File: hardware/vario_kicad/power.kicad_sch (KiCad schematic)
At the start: 28 parts, among them Q1 NMOS, Q2 PMOS, U4 USB C connector

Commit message: add missing footprints
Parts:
- R31, R32: footprint (none) -> Resistor_SMD:R_0402_1005Metric
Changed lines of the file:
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@@
 			)
 		)
-		(property "Footprint" ""
+		(property "Footprint" "Resistor_SMD:R_0402_1005Metric"
 			(at 148.082 72.39 90)
 			(effects
@@
 			)
 		)
-		(property "Footprint" ""
+		(property "Footprint" "Resistor_SMD:R_0402_1005Metric"
 			(at 132.08 38.608 90)
 			(effects

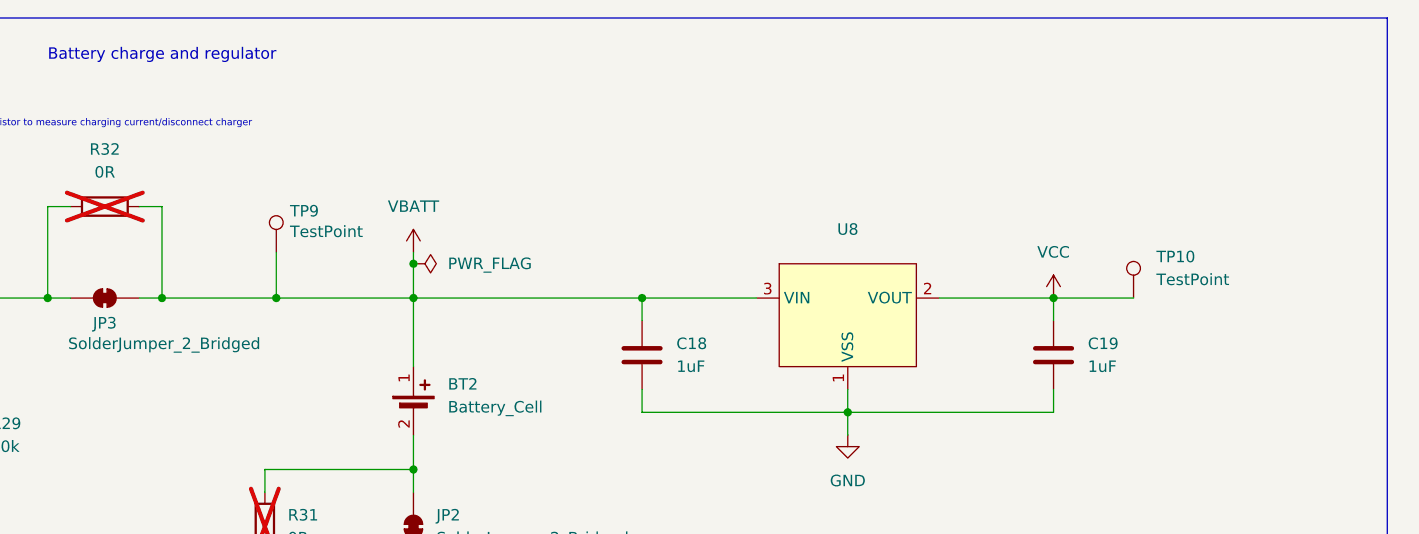
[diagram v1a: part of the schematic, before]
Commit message: remove more testpoints
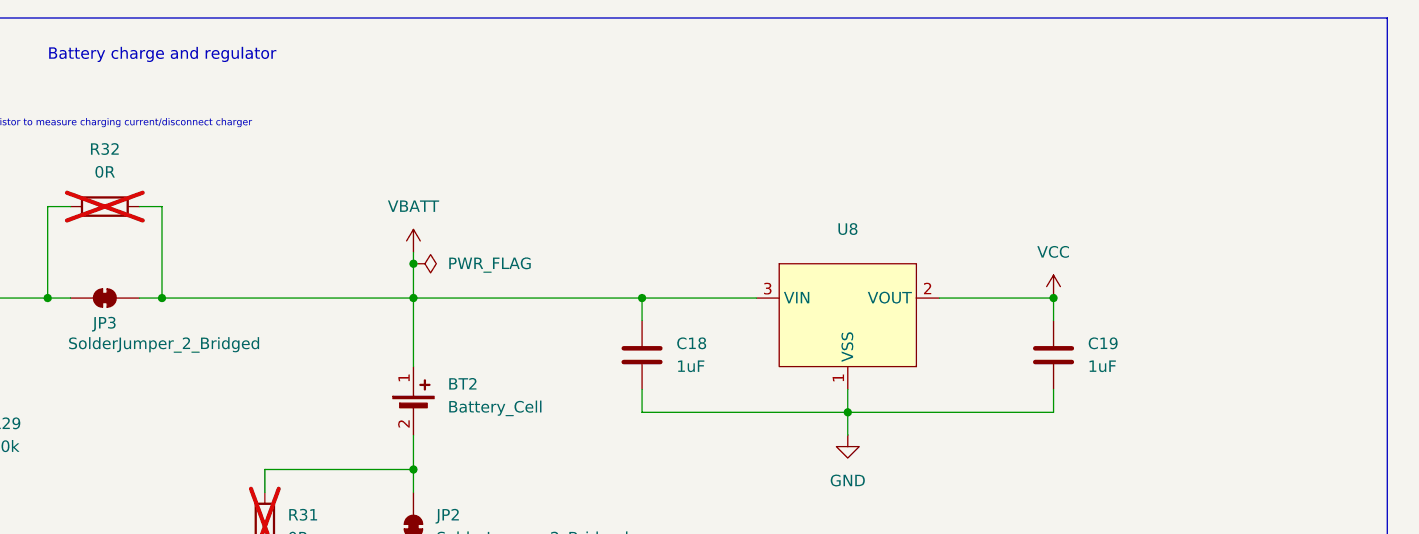
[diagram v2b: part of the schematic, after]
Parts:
- removed TP10, TP9: TestPoint, TestPoint:TestPoint_Pad_D1.0mm, symbol Connector:TestPoint
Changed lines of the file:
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@@
 	)
 	(junction
-		(at 151.13 46.99)
-		(diameter 0)
-		(color 0 0 0 0)
-	)
-	(junction
 		(at 76.2 29.21)
 		(diameter 0)
@@
 	(wire
 		(pts
-			(xy 151.13 41.91) (xy 151.13 46.99)
-		)
-		(stroke
-			(width 0)
-			(type default)
-		)
-	)
-	(wire
-		(pts
 			(xy 237.49 57.15) (xy 237.49 59.69)
 		)
@@
 	(wire
 		(pts
-			(xy 151.13 46.99) (xy 166.37 46.99)
-		)
-		(stroke
-			(width 0)
-			(type default)
-		)
-	)
-	(wire
-		(pts
 			(xy 68.58 137.16) (xy 68.58 140.97)
 		)
@@
 	(wire
 		(pts
-			(xy 237.49 46.99) (xy 246.38 46.99)
-		)
-		(stroke
-			(width 0)
-			(type default)
-		)
-	)
-	(wire
-		(pts
 			(xy 68.58 148.59) (xy 68.58 149.86)
 		)
@@
 	(wire
 		(pts
-			(xy 138.43 46.99) (xy 151.13 46.99)
+			(xy 138.43 46.99) (xy 166.37 46.99)
 		)
 		(stroke
@@
 	)
 	(symbol
-		(lib_id "Connector:TestPoint")
-		(at 246.38 46.99 0)
-		(unit 1)
-		(exclude_from_sim no)
-		(in_bom yes)
-		(on_board yes)
-		(dnp no)
-		(fields_autoplaced yes)
-		(property "Reference" "TP10"
-			(at 248.92 42.4179 0)
-			(effects
-				(font
-					(size 1.27 1.27)
-				)
-				(justify left)
-			)
-		)
-		(property "Value" "TestPoint"
-			(at 248.92 44.9579 0)
-			(effects
-				(font
-					(size 1.27 1.27)
-				)
-				(justify left)
-			)
-		)
-		(property "Footprint" "TestPoint:TestPoint_Pad_D1.0mm"
-			(at 251.46 46.99 0)
-			(effects
-				(font
-					(size 1.27 1.27)
-				)
-				(hide yes)
-			)
-		)
-		(property "Datasheet" "~"
-			(at 251.46 46.99 0)
-			(effects
-				(font
-					(size 1.27 1.27)
-				)
-				(hide yes)
-			)
-		)
-		(property "Description" "test point"
-			(at 246.38 46.99 0)
-			(effects
-				(font
-					(size 1.27 1.27)
-				)
-				(hide yes)
-			)
-		)
-		(property "Sim.Pins" ""
-			(at 246.38 46.99 0)
-			(effects
-				(font
-					(size 1.27 1.27)
-				)
-				(hide yes)
-			)
-		)
-		(pin "1"
-		)
-		(instances
-			(project "vario_kicad"
-				(path "/50389aff-b244-451e-8e3a-c5addd2215e1/9ff7b2dd-70fe-4259-884c-1f1f10c7ad3d"
-					(reference "TP10")
-					(unit 1)
-				)
-			)
-		)
-	)
-	(symbol
 		(lib_id "Device:R")
 		(at 132.08 36.83 90)
@@
 					(unit 1)
 				)
-			)
-		)
-	)
-	(symbol
-		(lib_id "Connector:TestPoint")
-		(at 151.13 41.91 0)
-		(unit 1)
-		(exclude_from_sim no)
-		(in_bom yes)
-		(on_board yes)
-		(dnp no)
-		(property "Reference" "TP9"
-			(at 152.654 37.338 0)
-			(effects
-				(font
-					(size 1.27 1.27)
-				)
-				(justify left)
-			)
-		)
-		(property "Value" "TestPoint"
-			(at 152.654 39.624 0)
-			(effects
-				(font
-					(size 1.27 1.27)
-				)
-				(justify left)
-			)
-		)
-		(property "Footprint" "TestPoint:TestPoint_Pad_D1.0mm"
-			(at 156.21 41.91 0)
-			(effects
-				(font
-					(size 1.27 1.27)
-				)
-				(hide yes)
-			)
-		)
-		(property "Datasheet" "~"
-			(at 156.21 41.91 0)
-			(effects
-				(font
-					(size 1.27 1.27)
-				)
-				(hide yes)
-			)
-		)
-		(property "Description" "test point"
-			(at 151.13 41.91 0)
-			(effects
-				(font
-					(size 1.27 1.27)
-				)
-				(hide yes)
-			)
-		)
-		(property "Sim.Pins" ""
-			(at 151.13 41.91 0)
-			(effects
-				(font
-					(size 1.27 1.27)
-				)
-				(hide yes)
-			)
-		)
-		(pin "1"
-		)
-		(instances
-			(project "vario_kicad"
-				(path "/50389aff-b244-451e-8e3a-c5addd2215e1/9ff7b2dd-70fe-4259-884c-1f1f10c7ad3d"
-					(reference "TP9")
-					(unit 1)
-				)

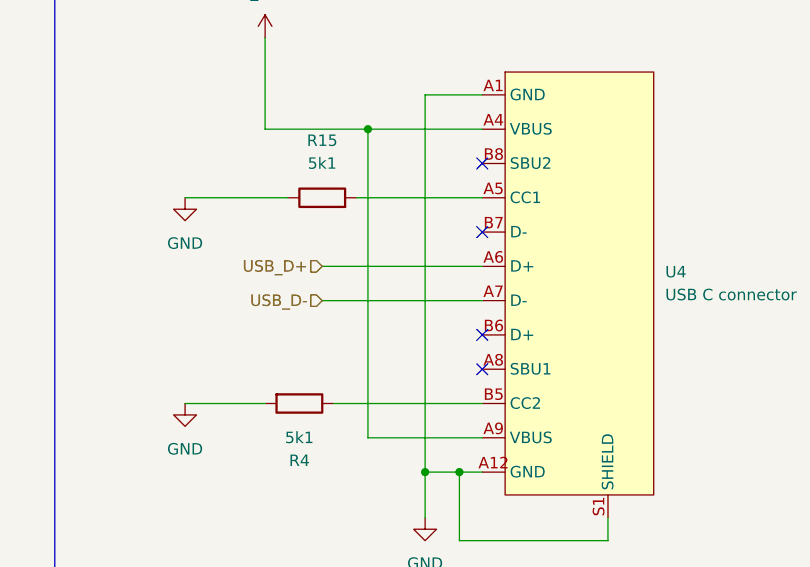
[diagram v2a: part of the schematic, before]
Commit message: use all 4 USB D+/- pins
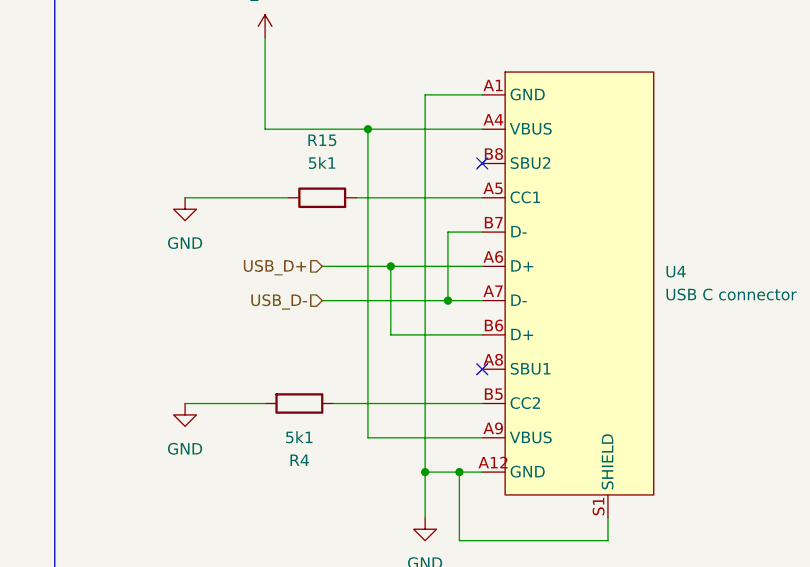
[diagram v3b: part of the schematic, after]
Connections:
- net USB_D+: now also U4.B6 (D+)
- net USB_D-: now also U4.B7 (D-)
- no-connect marks 4 -> 2
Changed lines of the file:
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@@
 	(paper "A4")
 	(junction
+		(at 156.21 133.35)
+		(diameter 0)
+		(color 0 0 0 0)
+	)
+	(junction
 		(at 88.9 29.21)
 		(diameter 0)
@@
 	(junction
 		(at 68.58 149.86)
+		(diameter 0)
+		(color 0 0 0 0)
+	)
+	(junction
+		(at 149.86 129.54)
 		(diameter 0)
 		(color 0 0 0 0)
@@
 		(at 160.02 118.11)
 	)
-	(no_connect
-		(at 160.02 137.16)
-	)
-	(no_connect
-		(at 160.02 125.73)
-	)
 	(wire
 		(pts
@@
 	(wire
 		(pts
+			(xy 156.21 133.35) (xy 160.02 133.35)
+		)
+		(stroke
+			(width 0)
+			(type default)
+		)
+	)
+	(wire
+		(pts
 			(xy 143.51 144.78) (xy 160.02 144.78)
 		)
@@
 	(wire
 		(pts
+			(xy 149.86 129.54) (xy 149.86 137.16)
+		)
+		(stroke
+			(width 0)
+			(type default)
+		)
+	)
+	(wire
+		(pts
 			(xy 173.99 157.48) (xy 173.99 160.02)
 		)
@@
 	(wire
 		(pts
+			(xy 156.21 125.73) (xy 156.21 133.35)
+		)
+		(stroke
+			(width 0)
+			(type default)
+		)
+	)
+	(wire
+		(pts
 			(xy 30.48 139.7) (xy 30.48 149.86)
 		)
@@
 	(wire
 		(pts
-			(xy 142.24 133.35) (xy 160.02 133.35)
+			(xy 142.24 133.35) (xy 156.21 133.35)
 		)
 		(stroke
@@
 	(wire
 		(pts
+			(xy 149.86 137.16) (xy 160.02 137.16)
+		)
+		(stroke
+			(width 0)
+			(type default)
+		)
+	)
+	(wire
+		(pts
 			(xy 166.37 62.23) (xy 166.37 66.04)
 		)
@@
 	(wire
 		(pts
+			(xy 160.02 125.73) (xy 156.21 125.73)
+		)
+		(stroke
+			(width 0)
+			(type default)
+		)
+	)
+	(wire
+		(pts
 			(xy 166.37 46.99) (xy 166.37 54.61)
 		)
@@
 	(wire
 		(pts
+			(xy 149.86 129.54) (xy 160.02 129.54)
+		)
+		(stroke
+			(width 0)
+			(type default)
+		)
+	)
+	(wire
+		(pts
 			(xy 147.32 114.3) (xy 147.32 148.59)
 		)
@@
 	(wire
 		(pts
-			(xy 142.24 129.54) (xy 160.02 129.54)
-		)
-		(stroke
+			(xy 142.24 129.54) (xy 149.86 129.54)
+		)
+		(stroke

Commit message: use 0402 instead of 0603 for almost all caps
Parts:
- C14, C18, C19: footprint Capacitor_SMD:C_0603_1608Metric -> Capacitor_SMD:C_0402_1005Metric
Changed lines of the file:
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@@
 			)
 		)
-		(property "Footprint" "Capacitor_SMD:C_0603_1608Metric"
+		(property "Footprint" "Capacitor_SMD:C_0402_1005Metric"
 			(at 238.4552 57.15 0)
 			(effects
@@
 			)
 		)
-		(property "Footprint" "Capacitor_SMD:C_0603_1608Metric"
+		(property "Footprint" "Capacitor_SMD:C_0402_1005Metric"
 			(at 64.4652 38.1 0)
 			(effects
@@
 			)
 		)
-		(property "Footprint" "Capacitor_SMD:C_0603_1608Metric"
+		(property "Footprint" "Capacitor_SMD:C_0402_1005Metric"
 			(at 192.7352 57.15 0)
 			(effects

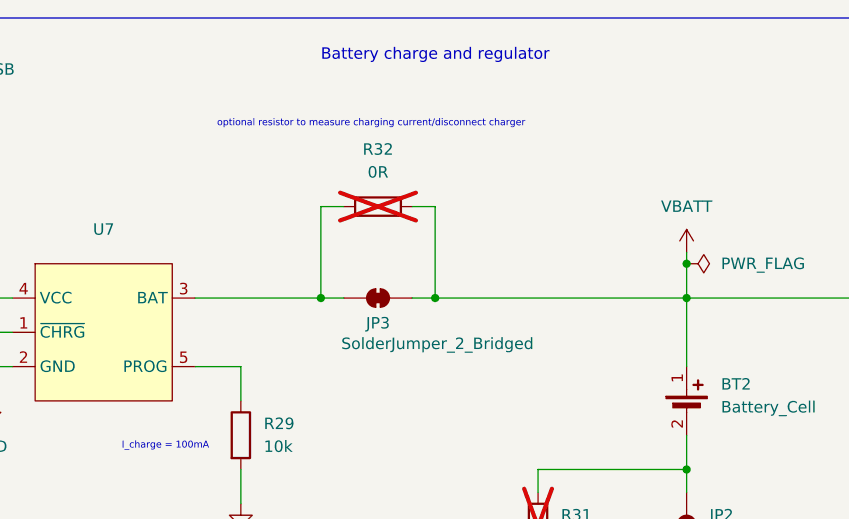
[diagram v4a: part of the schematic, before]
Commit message: remove jumper connecting charger to battery
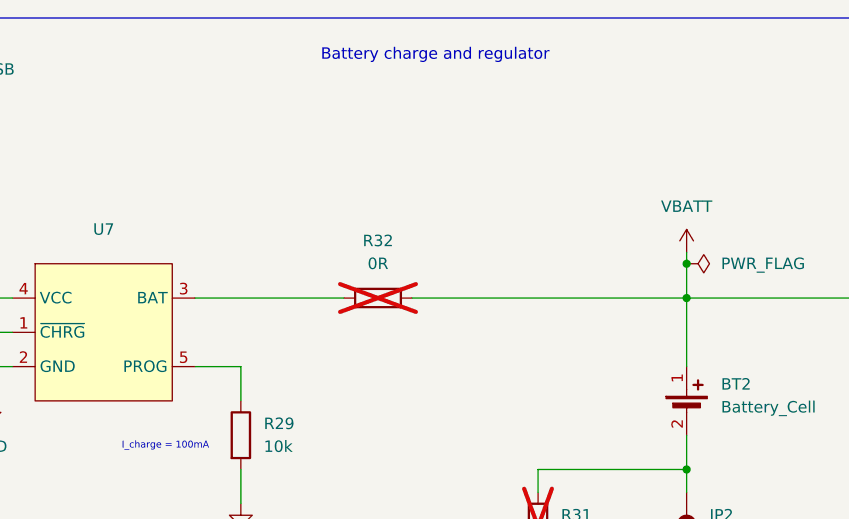
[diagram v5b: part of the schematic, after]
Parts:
- removed JP3: SolderJumper_2_Bridged, Jumper:SolderJumper-2_P1.3mm_Open_TrianglePad1.0x1.5mm, symbol Jumper:SolderJumper_2_Bridged
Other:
- note removed: "optional resistor to measure charging current/disconnect charger"
- moved on the sheet: R32
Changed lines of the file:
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@@
 	)
 	(junction
-		(at 138.43 46.99)
-		(diameter 0)
-		(color 0 0 0 0)
-	)
-	(junction
 		(at 166.37 78.74)
 		(diameter 0)
@@
 	)
 	(junction
-		(at 125.73 46.99)
-		(diameter 0)
-		(color 0 0 0 0)
-	)
-	(junction
 		(at 41.91 149.86)
 		(diameter 0)
@@
 	(wire
 		(pts
-			(xy 128.27 46.99) (xy 125.73 46.99)
-		)
-		(stroke
-			(width 0)
-			(type default)
-		)
-	)
-	(wire
-		(pts
 			(xy 153.67 110.49) (xy 160.02 110.49)
 		)
@@
 	(wire
 		(pts
-			(xy 128.27 36.83) (xy 125.73 36.83)
-		)
-		(stroke
-			(width 0)
-			(type default)
-		)
-	)
-	(wire
-		(pts
 			(xy 30.48 149.86) (xy 41.91 149.86)
 		)
@@
 	(wire
 		(pts
-			(xy 125.73 36.83) (xy 125.73 46.99)
-		)
-		(stroke
-			(width 0)
-			(type default)
-		)
-	)
-	(wire
-		(pts
 			(xy 214.63 59.69) (xy 214.63 62.23)
 		)
@@
 	(wire
 		(pts
-			(xy 138.43 46.99) (xy 135.89 46.99)
-		)
-		(stroke
-			(width 0)
-			(type default)
-		)
-	)
-	(wire
-		(pts
 			(xy 30.48 118.11) (xy 43.18 118.11)
 		)
@@
 	(wire
 		(pts
-			(xy 138.43 46.99) (xy 166.37 46.99)
-		)
-		(stroke
-			(width 0)
-			(type default)
-		)
-	)
-	(wire
-		(pts
-			(xy 138.43 36.83) (xy 135.89 36.83)
+			(xy 135.89 46.99) (xy 166.37 46.99)
 		)
 		(stroke
@@
 	(wire
 		(pts
-			(xy 111.76 46.99) (xy 125.73 46.99)
+			(xy 111.76 46.99) (xy 128.27 46.99)
 		)
 		(stroke
@@
 	(wire
 		(pts
-			(xy 138.43 46.99) (xy 138.43 36.83)
-		)
-		(stroke
-			(width 0)
-			(type default)
-		)
-	)
-	(wire
-		(pts
 			(xy 166.37 76.2) (xy 166.37 78.74)
 		)
@@
 		)
 	)
-	(text "optional resistor to measure charging current/disconnect charger"
-		(exclude_from_sim no)
-		(at 131.318 27.686 0)
-		(effects
-			(font
-				(size 0.762 0.762)
-			)
-		)
-	)
 	(text "Max V_BATT voltage 4.3V\nmax adc voltage 2.15V"
 		(exclude_from_sim no)
@@
 	)
 	(symbol
-		(lib_id "Jumper:SolderJumper_2_Bridged")
-		(at 132.08 46.99 0)
-		(unit 1)
-		(exclude_from_sim yes)
-		(in_bom no)
-		(on_board yes)
-		(dnp no)
-		(property "Reference" "JP3"
-			(at 132.08 49.784 0)
-			(effects
-				(font
-					(size 1.27 1.27)
-				)
-			)
-		)
-		(property "Value" "SolderJumper_2_Bridged"
-			(at 138.684 52.07 0)
-			(effects
-				(font
-					(size 1.27 1.27)
-				)
-			)
-		)
-		(property "Footprint" "Jumper:SolderJumper-2_P1.3mm_Open_TrianglePad1.0x1.5mm"
-			(at 132.08 46.99 0)
-			(effects
-				(font
-					(size 1.27 1.27)
-				)
-				(hide yes)
-			)
-		)
-		(property "Datasheet" "~"
-			(at 132.08 46.99 0)
-			(effects
-				(font
-					(size 1.27 1.27)
-				)
-				(hide yes)
-			)
-		)
-		(property "Description" "Solder Jumper, 2-pole, closed/bridged"
-			(at 132.08 46.99 0)
-			(effects
-				(font
-					(size 1.27 1.27)
-				)
-				(hide yes)
-			)
-		)
-		(pin "1"
-		)
-		(pin "2"
-		)
-		(instances
-			(project "vario_kicad"
-				(path "/50389aff-b244-451e-8e3a-c5addd2215e1/9ff7b2dd-70fe-4259-884c-1f1f10c7ad3d"
-					(reference "JP3")
-					(unit 1)
-				)
-			)
-		)
-	)
-	(symbol
 		(lib_id "Device:C")
 		(at 237.49 53.34 0)
@@
 	(symbol
 		(lib_id "Device:R")
-		(at 132.08 36.83 90)
+		(at 132.08 46.99 90)
 		(unit 1)
 		(exclude_from_sim no)
@@
 		(fields_autoplaced yes)
 		(property "Reference" "R32"
-			(at 132.08 30.48 90)
+			(at 132.08 40.64 90)
 			(effects
 				(font
@@
 		)
 		(property "Value" "0R"
-			(at 132.08 33.02 90)
+			(at 132.08 43.18 90)
 			(effects
 				(font
@@
 		)
 		(property "Footprint" "Resistor_SMD:R_0402_1005Metric"
-			(at 132.08 38.608 90)
+			(at 132.08 48.768 90)
 			(effects
 				(font
@@
 		)
 		(property "Datasheet" "~"
-			(at 132.08 36.83 0)
+			(at 132.08 46.99 0)
 			(effects
 				(font
@@
 		)
 		(property "Description" "Resistor"
-			(at 132.08 36.83 0)
+			(at 132.08 46.99 0)
 			(effects
 				(font
